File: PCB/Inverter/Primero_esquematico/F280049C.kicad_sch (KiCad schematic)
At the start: 1 part, among them U21 F280049CPZS

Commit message: Esquematico practicamente terminado
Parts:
- added C100, C101, C102, C109, C110, C99: 2.2uF, Capacitor_SMD:C_0603_1608Metric, symbol Device:C_Small
- added C103, C104, C105, C108, C111, C92, C93, C94, C95, C97, C98: 100nF, Capacitor_SMD:C_0603_1608Metric, symbol Device:C_Small
- added C106, C107: 10pF, Capacitor_SMD:C_0402_1005Metric, symbol Device:C_Small
- added C90, C91, C96: 10uF, Capacitor_SMD:C_0805_2012Metric, symbol Device:C_Small
- added D60, D61, D62: APT2012EC, LED_SMD:LED_0805_2012Metric, symbol Device:LED
- added R178: 60, Resistor_SMD:R_0402_1005Metric, symbol Device:R_Small
- added R179, R180: 0, Resistor_SMD:R_0402_1005Metric, symbol Device:R_Small
- added R182: 10k, Resistor_SMD:R_0402_1005Metric, symbol Device:R_Small
- added R187, R188, R189: 1k5, Resistor_SMD:R_0402_1005Metric, symbol Device:R
- added U30: TPS3823-33DBVR, Snapeda:DBV5-L, symbol Snapeda:TPS3823-33DBVR
- added Y1: ABM8GAIG-20.000MHZ-8-7Z-T3, Snapeda:XTAL_ABM8GAIG-20.000MHZ-8-7Z-T3, symbol Snapeda:ABM8GAIG-20.000MHZ-8-7Z-T3
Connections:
- net GP_28_UART_RX: now reaches U21.1 (GPIO28)
- net GP_29_UART_TX: now reaches U21.100 (GPIO29)
- net GP_13_Encoder_Z: now reaches U21.50 (GPIO13)
- net GP_11_Encoder_B: now reaches U21.52 (GPIO11)
- net GP_16_OverDC: now reaches U21.54 (GPIO16)
- net GP_17_GD_FLT: now reaches U21.55 (GPIO17)
- net GP_24_BOOT_MODE_2: now reaches U21.56 (GPIO24)
- net GP_25_Encoder_SSI_Data: now reaches U21.57 (GPIO25)
- net GP_26_LED_A: now reaches U21.58 (GPIO26)
- net GP_26_LED_A: now also R188.1
- net GP_27_LED_B: now reaches U21.59 (GPIO27)
- net GP_27_LED_B: now also R189.1
- net GPIO18_X2: now reaches U21.68 (GPIO18_X2)
- net GPIO18_X2: now also C107.1, Y1.1
- net GP_8_CAN_B_TX: now reaches U21.74 (GPIO08)
- net GP_4_PWM_MP_H_C: now reaches U21.75 (GPIO04)
- net GP_3_PWM_MP_L_B: now reaches U21.76 (GPIO03)
- net GP_2_PWM_MP_H_B: now reaches U21.77 (GPIO02)
- net GP_1_PWM_MP_L_A: now reaches U21.78 (GPIO01)
- net GP_0_PWM_MP_H_A: now reaches U21.79 (GPIO00)
- net GP_23_LED_C: now reaches U21.81 (GPIO23_SW)
- net GP_23_LED_C: now also R187.1
- net GP_22_Encoder_SSI_CLK: now reaches U21.83 (GPIO22_SW)
- net GP_7_CAN_B_RX: now reaches U21.84 (GPIO07)
- net GP_5_PWM_MP_L_C: now reaches U21.89 (GPIO05)
- net GP_9_OverCurrent_MP_A: now reaches U21.90 (GPIO09)
- net GP_10_Encoder_A: now reaches U21.93 (GPIO10)
- net GP_15_OverCurrent_MP_C: now reaches U21.95 (GPIO15)
- net GP_14_OverCurrent_MP_B: now reaches U21.96 (GPIO14)
- net GP_6_PWM_FAN: now reaches U21.97 (GPIO06)
- net GP_30_CAN_A_RX: now reaches U21.98 (GPIO30)
- net GP_31_CAN_A_TX: now reaches U21.99 (GPIO31)
- net TDO: now reaches U21.61 (GPIO37_TDO)
- net TDI: now reaches U21.63 (GPIO35_TDI)
- net GP_32_BOOT_MODE_1: now reaches U21.64 (GPIO32)
- net GP_58_WD: now reaches U21.67 (GPIO58)
- net GP_58_WD: now also U30.4 (WDI)
- net GP_40_GD_RDY: now reaches U21.85 (GPIO40)
- net GP_39_E_STOP: now reaches U21.91 (GPIO39)
- net GP_34_Reset_Pote: now reaches U21.94 (GPIO34)
- net Reset_MCU: now reaches U21.2 (XRS_N)
- net Reset_MCU: now also C108.1, R182.2, U30.1 (*RESET)
- net at U21.48 (FLT2): now also R180.1
- net at U21.49 (FLT1): now also R179.1
- net TCK: now reaches U21.60 (TCK)
- net TMS: now reaches U21.62 (TMS)
- net X1: now reaches U21.69 (X1)
- net X1: now also C106.1, Y1.3
- net GND: now reaches U21.73 (VREGENZ)
- net GND: now also U21.12 (VSSA), U21.13 (PGA5_GND), U21.14 (PGA1_GND), U21.15 (PGA3_GND), U21.26 (VREFLOB_VREFLOC), U21.27 (VREFLOA), U21.32 (PGA2_GND_PGA4_GND_PGA6_GND), U21.33 (VSSA), U21.42 (PGA7_GND), U21.45 (VSS), U21.5 (VSS), U21.72 (VSS), U21.82 (VSS_SW), U21.86 (VSS), C100.2, C101.2, C102.2, C103.2, C104.2, C105.2, C106.2, C107.2, C108.2, C109.2, C110.2, C111.2, C90.1, C91.1, C92.1, C93.1, C94.1, C95.1, C96.2, C97.2, C98.2, C99.2, D60.1 (K), D61.1 (K), D62.1 (K), U30.2 (GND)
- net A3_Tension_MP_A: now reaches U21.10 (A3)
- net C4_Temp_PCB: now reaches U21.17 (C4)
- net C0_Current_MP_C: now reaches U21.19 (C0)
- net C2_Temp_MP_C: now reaches U21.21 (C2)
- net A0_Current_MP_A: now reaches U21.23 (A0_B15_C15_DACA_OUT)
- net +3V0: now reaches U21.24 (VREFHIB_VREFHIC)
- net +3V0: now also U21.25 (VREFHIA), C109.1, C110.1
- net C1_Tension_MP_C: now reaches U21.29 (C1)
- net A5_Tension_DC: now reaches U21.35 (A5)
- net A8_5V_C_SP: now reaches U21.37 (A8_PGA6_OF)
- net B4_Temp_MP_B: now reaches U21.39 (B4_C8_PGA4_OF)
- net B1_Tension_MP_B: now reaches U21.40 (B1_A10_C10_PGA7_OF)
- net B0_Current_MP_B: now reaches U21.41 (B0)
- net A6_ADC_PS: now reaches U21.6 (A6_PGA5_OF)
- net B2_Temp_MP_A: now reaches U21.7 (B2_C6_PGA3_OF)
- net at U21.11 (VDDA): now also U21.34 (VDDA), C100.1, C101.1, C102.1, R178.2
- net at U21.3 (VDDIO): now also U21.47 (VDDIO), U21.70 (VDDIO), U21.80 (VDDIO_SW), U21.88 (VDDIO), C103.1, C104.1, C105.1, C96.1, C97.1, C98.1
- net at U21.4 (VDD): now also U21.46 (VDD), U21.71 (VDD), U21.87 (VDD), C90.2, C91.2, C92.2, C93.2, C94.2, C95.2
- new net: Y1.2 (NC), Y1.4 (NC__1)
- new net: D61.2 (A), R188.2
- new net: D60.2 (A), R187.2
- new net: D62.2 (A), R189.2
- new net +3.3VP: C111.1, C99.1, R178.1, R182.1, U30.3 (*MR), U30.5 (VDD)
- new net Hardware_error: R179.2
- new net Stop_Button: R180.2
- no-connect marks 0 -> 17
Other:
- note added: "El pin 2 se tiro directoa tirerra en lugar de colocar un sistema que regula la tension de alimentacion por temas de costos y esapacio (en caso de volverlo comersial se tendria que evaluar incorporar este componente)"
- note added: "Este es un WatchDog externo"
- note added: "FLTX es una entrada que al conectarse y detectar un error apaga dirrectametne el PWM del micro. Esto funciona de manera asincronica asegurando el menor tiempo de respuesta (aprox 100ns) Sirve para cosas de ultra prioridad y seguridad"
- note added: "Led de Estado"
- note added: "PGAs internos (Programmable Gain Amplifiers)"
- moved on the sheet: U21A, U21B, U21C, U21D, U21E

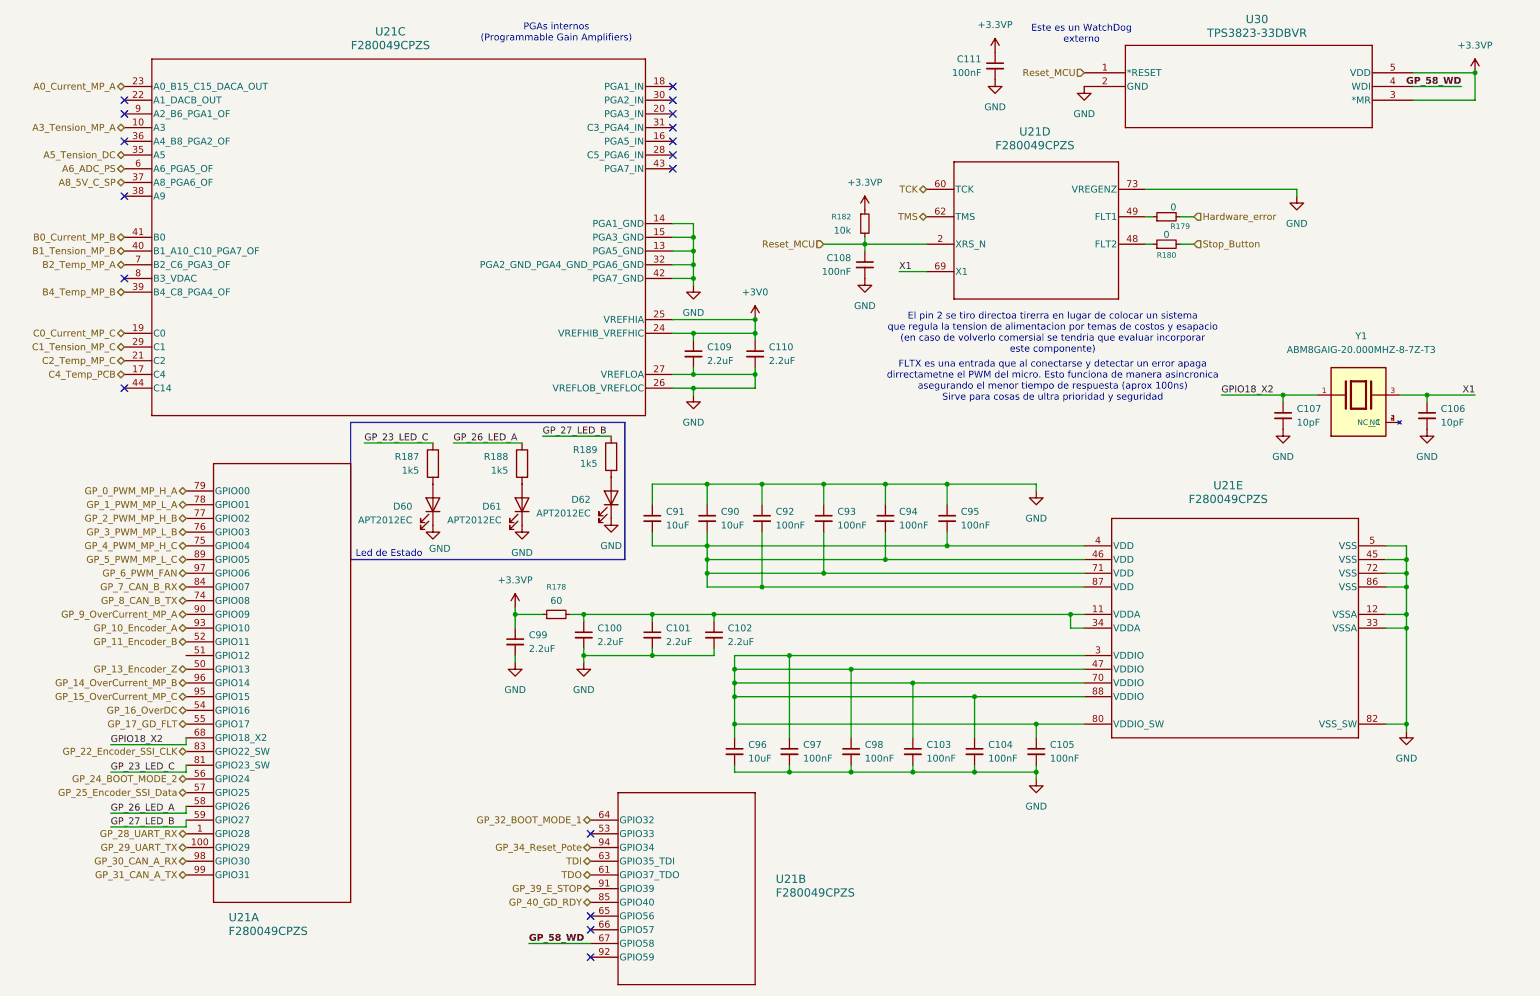
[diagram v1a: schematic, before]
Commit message: Un par de cosas q corregi del ERC pero sigue mal
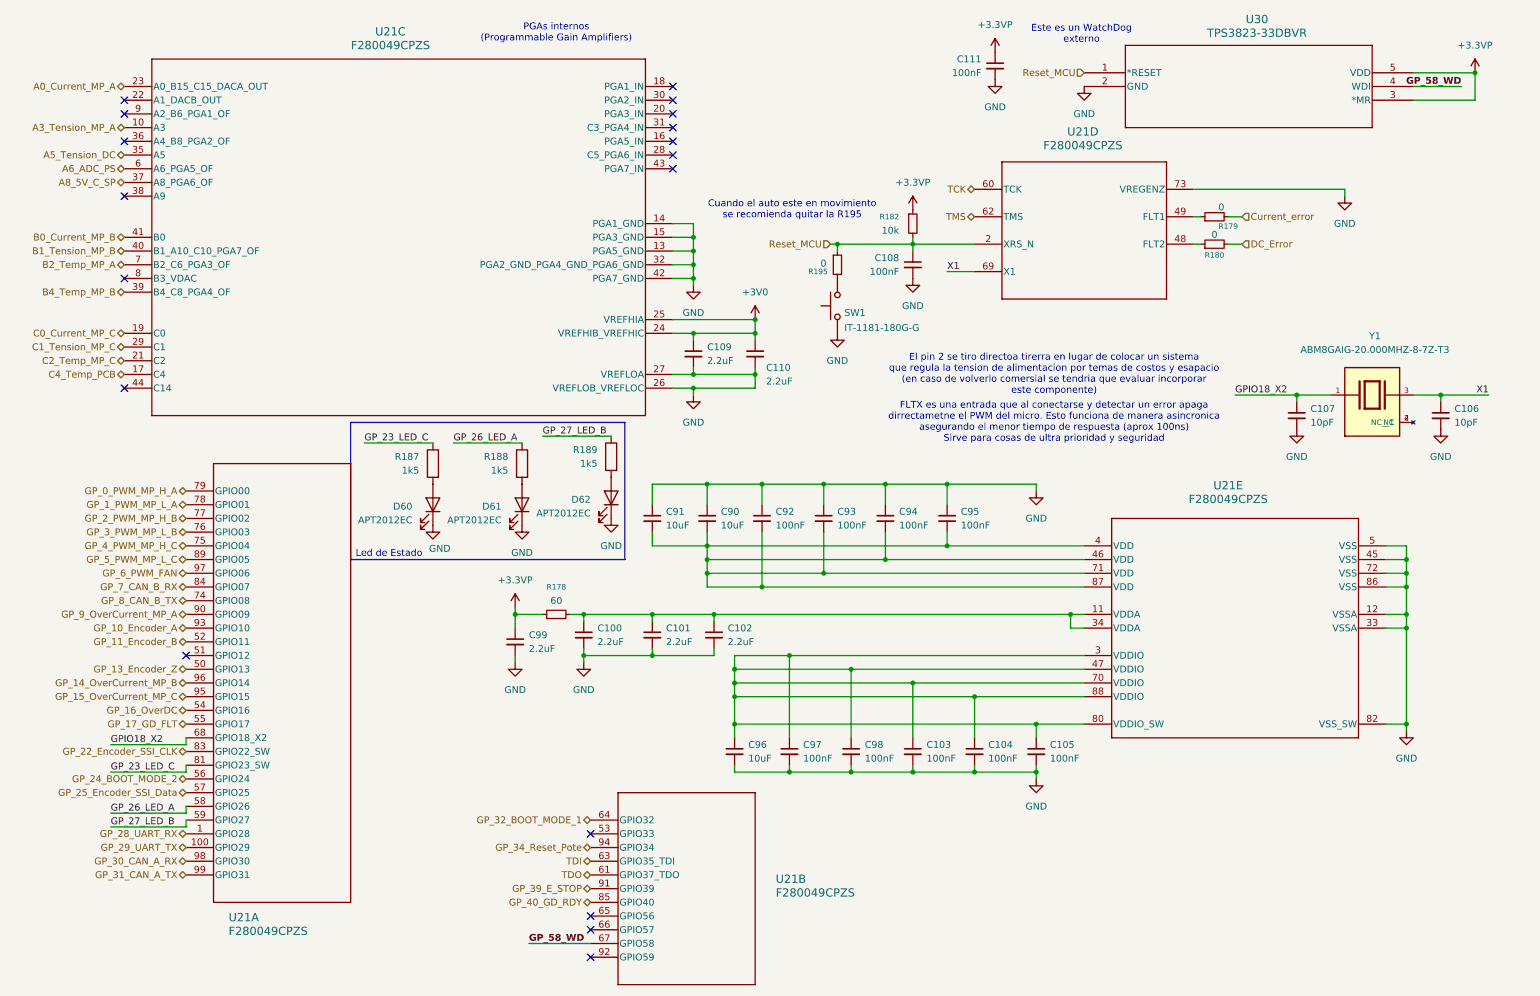
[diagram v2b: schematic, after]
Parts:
- added R195: 0, Resistor_SMD:R_0402_1005Metric, symbol Device:R_Small
- added SW1: IT-1181-180G-G, FSAE_footprints:Sin título, symbol Switch:SW_Push
- U21: footprint Snapeda:PZ0100A_L -> PZ0100A_N
- U30: footprint Snapeda:DBV5-L -> DBV5
- Y1: footprint Snapeda:XTAL_ABM8GAIG-20.000MHZ-8-7Z-T3 -> ABM8GAIG-20.000MHZ-8-7Z-T3:XTAL_ABM8GAIG-20.000MHZ-8-7Z-T3
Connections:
- net GND: now also SW1.1
- net Reset_MCU: now also R195.1
- net Hardware_error renamed Current_error
- net Stop_Button renamed DC_Error
- new net: R195.2, SW1.2
- no-connect marks 17 -> 18
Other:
- note added: "Cuando el auto este en movimiento se recomienda quitar la R195"
- moved on the sheet: C106, C107, C108, R179, R180, R182, U21D, Y1

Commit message: Esquematico Listo
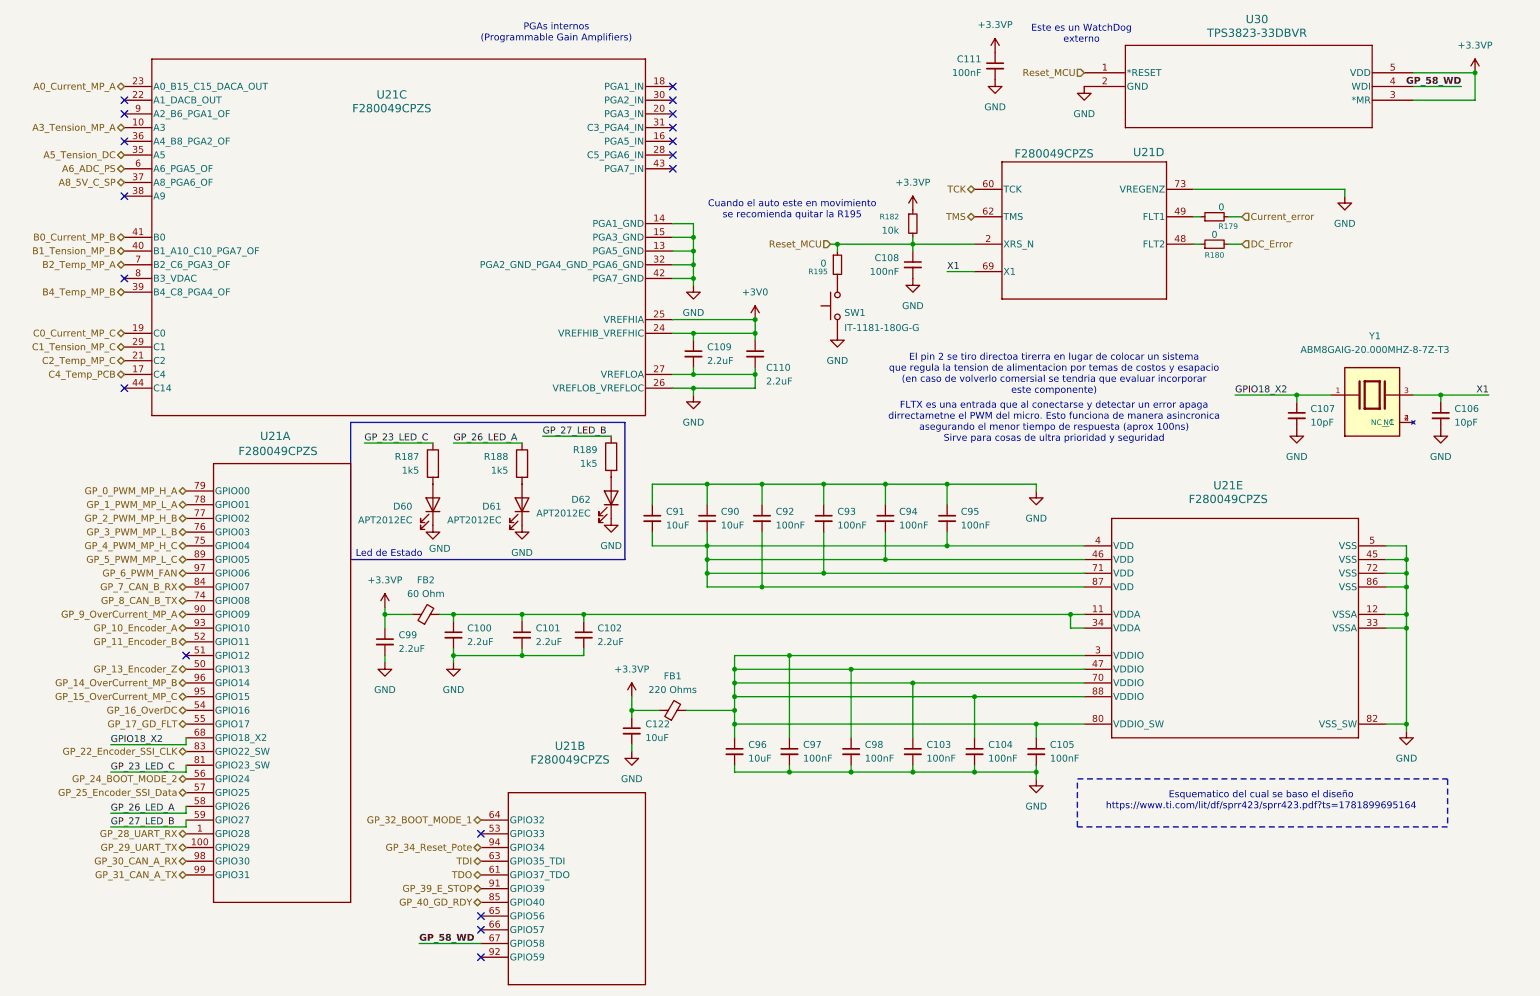
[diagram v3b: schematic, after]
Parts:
- removed R178: 60, Resistor_SMD:R_0402_1005Metric, symbol Device:R_Small
- added C122: 10uF, Capacitor_SMD:C_0603_1608Metric, symbol Device:C_Small
- added FB1: 220 Ohms, Inductor_SMD:L_01005_0402Metric_Pad0.57x0.30mm_HandSolder, symbol Device:FerriteBead_Small
- added FB2: 60 Ohm, Inductor_SMD:L_01005_0402Metric_Pad0.57x0.30mm_HandSolder, symbol Device:FerriteBead_Small
- U21: footprint PZ0100A_N -> Snapeda:PZ0100A_L
- U30: footprint DBV5 -> Snapeda:DBV5-L
- Y1: footprint ABM8GAIG-20.000MHZ-8-7Z-T3:XTAL_ABM8GAIG-20.000MHZ-8-7Z-T3 -> Snapeda:XTAL_ABM8GAIG-20.000MHZ-8-7Z-T3
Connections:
- net +3.3VP: now also C122.1, FB1.1, FB2.1
- net GND: now also C122.2
- net at C103.1, C104.1, C105.1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: now also FB1.2
- net at C100.1, C101.1, C102.1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: now also FB2.2
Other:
- note added: "Esquematico del cual se baso el diseño https://www.ti.com/lit/df/sprr423/sprr423.pdf?ts=1781899695164"
- moved on the sheet: C100, C101, C102, C99, U21B

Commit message: correcciones
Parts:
- FB1: renamed from FB2; footprint Inductor_SMD:L_01005_0402Metric_Pad0.57x0.30mm_HandSolder -> Inductor_SMD:L_0402_1005Metric_Pad0.77x0.64mm_HandSolder
- FB2: renamed from FB1; footprint Inductor_SMD:L_01005_0402Metric_Pad0.57x0.30mm_HandSolder -> Inductor_SMD:L_0402_1005Metric_Pad0.77x0.64mm_HandSolder
- renumbered C104 to C100, C111 to C101, C105 to C102, C107 to C103, C106 to C104, C99 to C82, C100 to C83, C101 to C84, C102 to C85, C122 to C86, C91 to C87, C109 to C88, C90 to C89, C96 to C90, C110 to C91, C97 to C93, C93 to C94, C98 to C95, C94 to C96, C108 to C97, C103 to C98, C95 to C99, D60 to D72, D61 to D73, D62 to D74, R187 to R93, R188 to R94, R189 to R95, R195 to R96, R182 to R97, R179 to R98, R180 to R99, U21 to U15, U30 to U16

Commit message: Algunos cambios
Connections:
- net +3.3VP renamed +3.3_digital
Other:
- moved on the sheet: C101

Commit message: Corregi cosas de la placa
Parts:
- renumbered C82 to C101, C83 to C102, C84 to C103, C85 to C104, C86 to C105, C87 to C106, C88 to C107, C89 to C108, C90 to C109, C91 to C110, C92 to C111, C93 to C112, C94 to C113, C95 to C114, C96 to C115, C97 to C116, C98 to C117, C99 to C118, C101 to C119, C100 to C120, C102 to C121, C103 to C122, C104 to C123

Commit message: a
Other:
- note added: "Esquematico del cual se baso el diseño https://www.ti.com/lit/df/sprr423/sprr423.pdf?ts=1781899695164 https://www.ti.com/tool/es-mx/LAUNCHXL-F280049C"
- note removed: "Esquematico del cual se baso el diseño https://www.ti.com/lit/df/sprr423/sprr423.pdf?ts=1781899695164"

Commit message: Modificaciones varias
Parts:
- SW1: value IT-1181-180G-G -> IT-1187-160GM-G; footprint FSAE_footprints:Sin título -> FSAE_footprints:IT-1187-160GM-G; Compra https://electrocomponentes.com/tienda/componentes-electronicos/interruptores/tact-switch-smd-it-1181-180g-g-tr -> https://electrocomponentes.com/tienda/componentes-electronicos/interruptores/tact-switch-smd-it-1187-160gm-g
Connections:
- net GP_12_CAN_B_TX: now reaches U15.51 (GPIO12)
- net GP_13_Encoder_Z renamed GP_13_CAN_B_RX
- net GP_14_OverCurrent_MP_B renamed GP_14_OverCurrent_MP_A
- net GP_15_OverCurrent_MP_C renamed GP_15_OverCurrent_MP_B
- net GP_16_OverDC renamed GP_16_OverCurrent_MP_C
- net GP_17_GD_FLT renamed GP_17_OverDC
- net GP_22_Encoder_SSI_CLK renamed GP_22_GD_FLT
- net GP_23_LED_C: no longer names the net of U15.81 (GPIO23_SW)
- net GP_23_LED_C: no longer R93.1
- net GP_25_Encoder_SSI_Data renamed GP_25_LED_A
- net GP_25_LED_A: now also R93.1
- net GP_26_LED_A renamed GP_26_LED_B
- net GP_27_LED_B renamed GP_27_LED_C
- net GP_7_CAN_B_RX renamed GP_7_Encoder_SSI_Data
- net GP_8_CAN_B_TX renamed GP_8_Encoder_SSI_CLK
- net GP_9_OverCurrent_MP_A renamed GP_9_Encoder_Z
